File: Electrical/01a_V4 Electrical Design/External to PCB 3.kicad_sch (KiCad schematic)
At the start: 1 part, among them J1000 Dupont 2x2

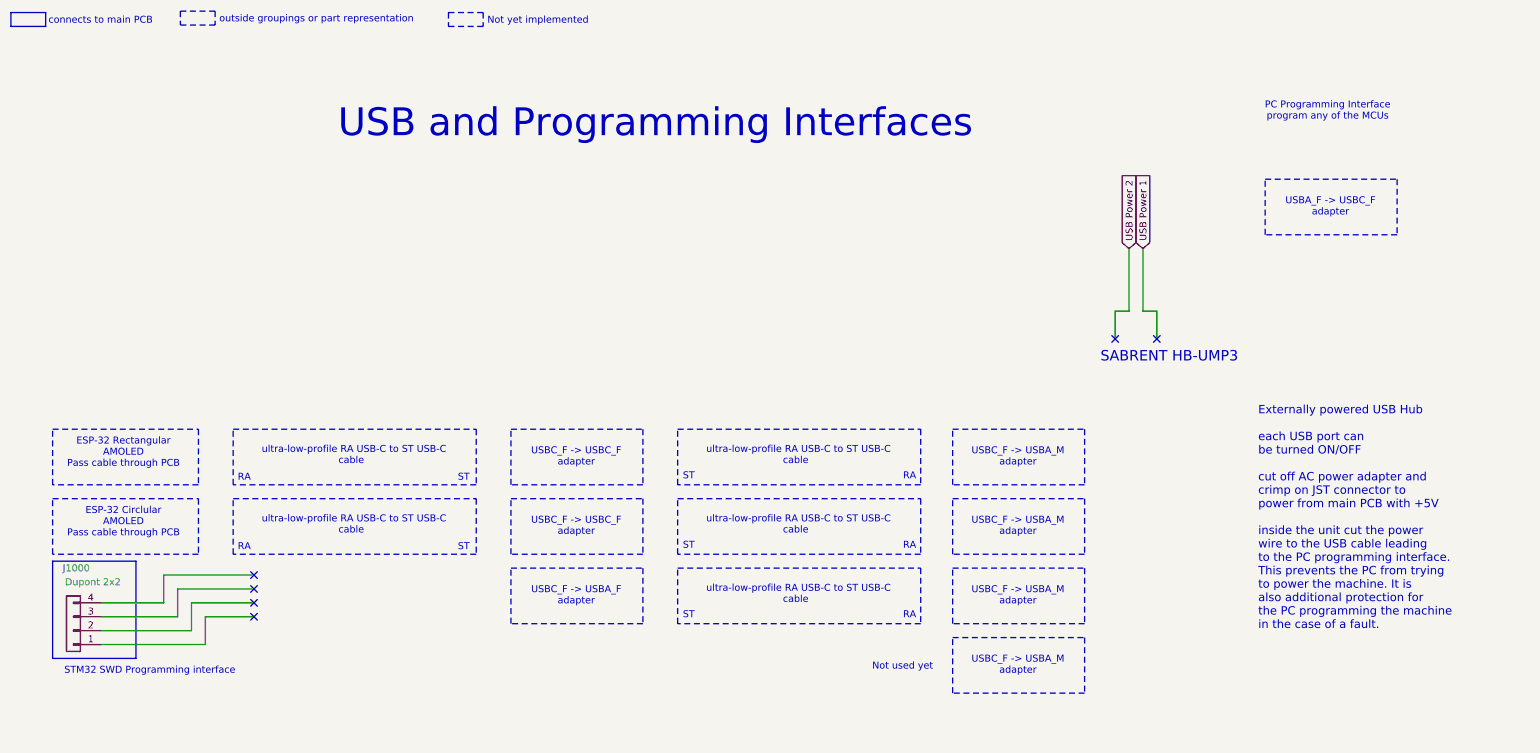
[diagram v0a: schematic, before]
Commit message: main schematic tweaks. Started the 'Saber' PCB which is the new end effector for the strobe light. Schematic nearly finished. Need to create footprint for LEDs and layout the board to be CNC milled.
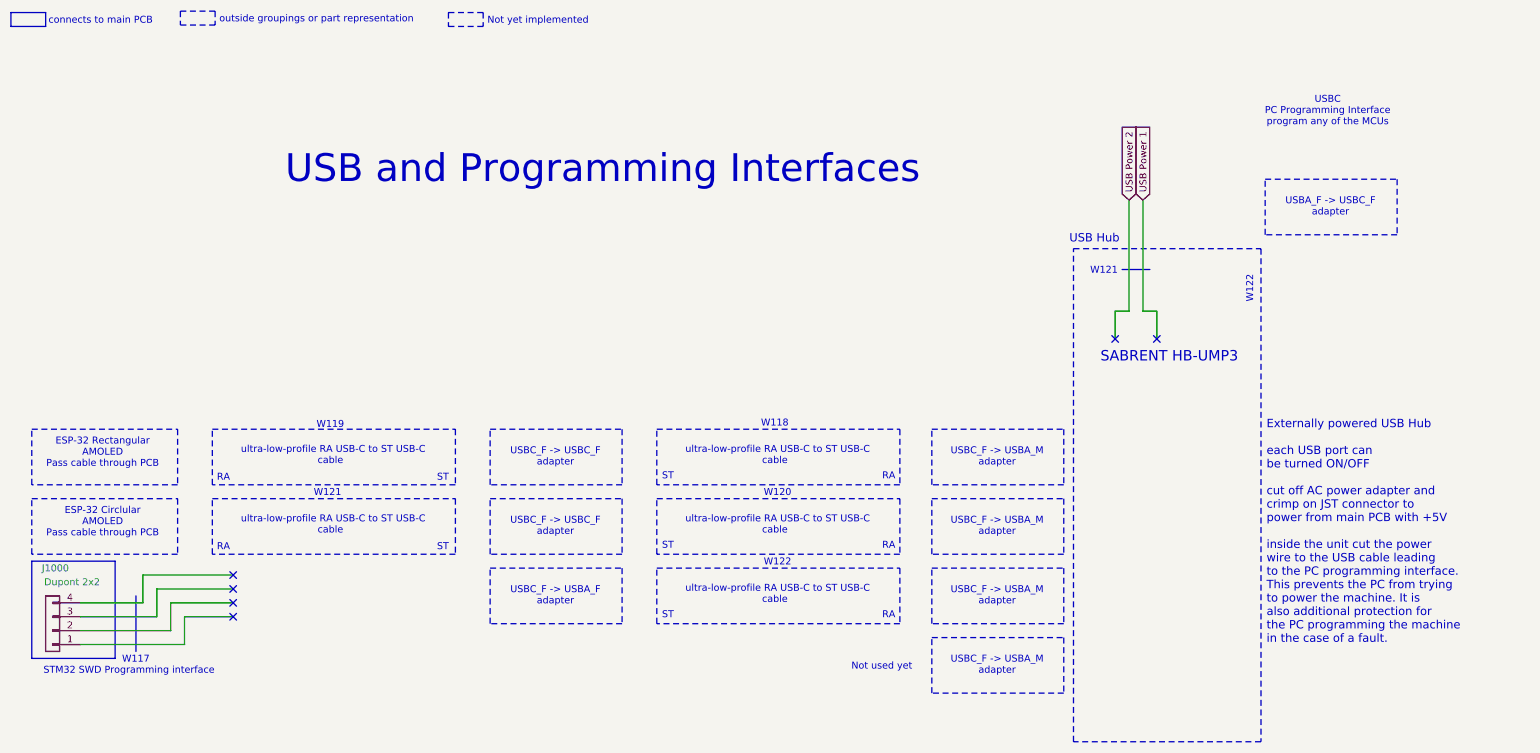
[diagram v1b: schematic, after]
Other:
- note added: "USB Hub"
- note added: "USBC PC Programming Interface program any of the MCUs"
- note added: "W117"
- note added: "W118"
- note added: "W119"
- note added: "W120"
- note added: "W121"
- note added: "W122"
- note removed: "PC Programming Interface program any of the MCUs"
- company: (none) -> Kadin Whiting
- title: (none) -> External Devices 3
- moved on the sheet: J1000
